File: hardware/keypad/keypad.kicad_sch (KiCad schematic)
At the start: 7 parts, among them J101 Conn_02x05_Odd_Even

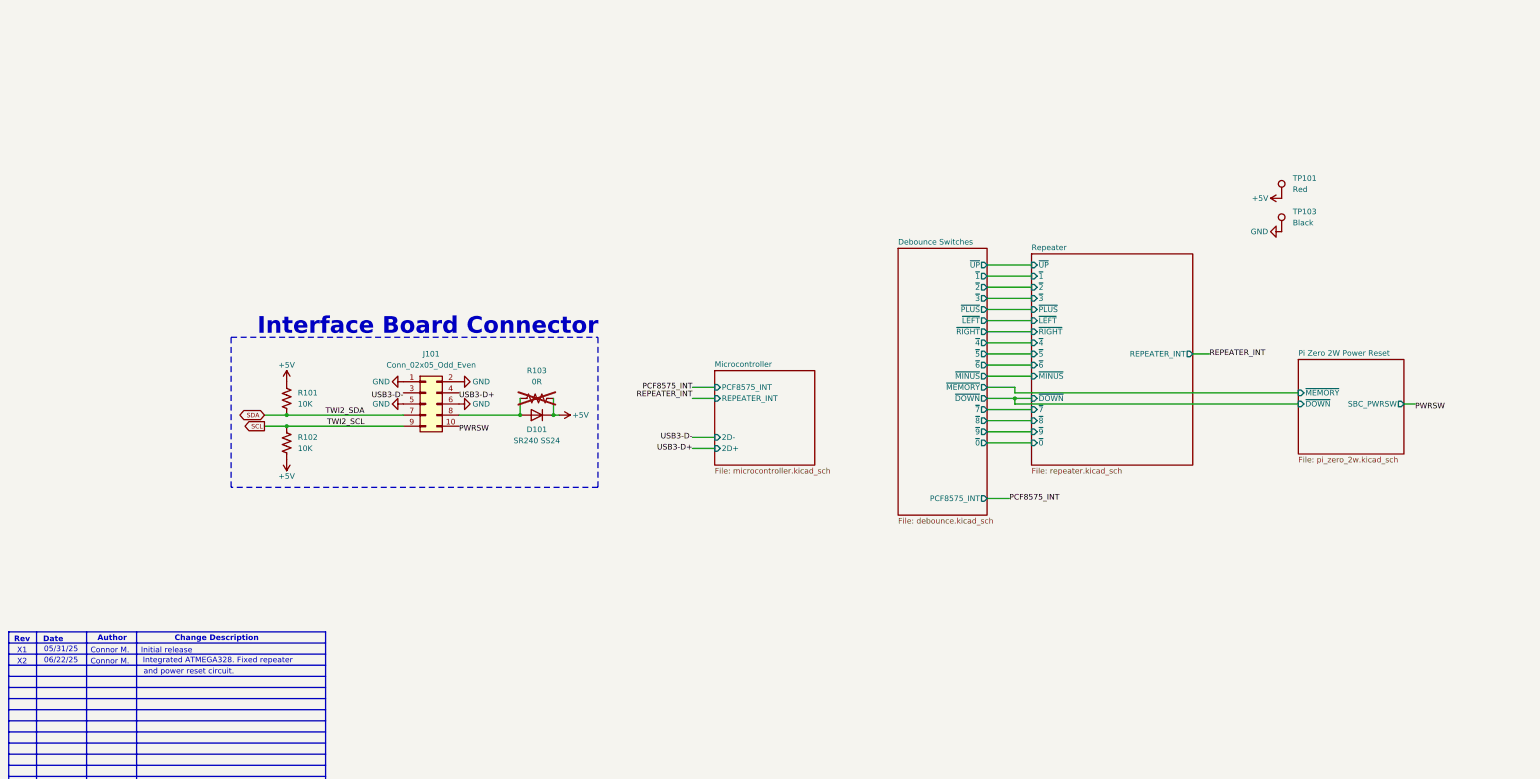
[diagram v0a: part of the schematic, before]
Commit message: [fix] repeater and sbc shutdown circuit
Fixed repeater and SBC shutdown circuit. Switched +5V VCC to +3.3V. Added C211
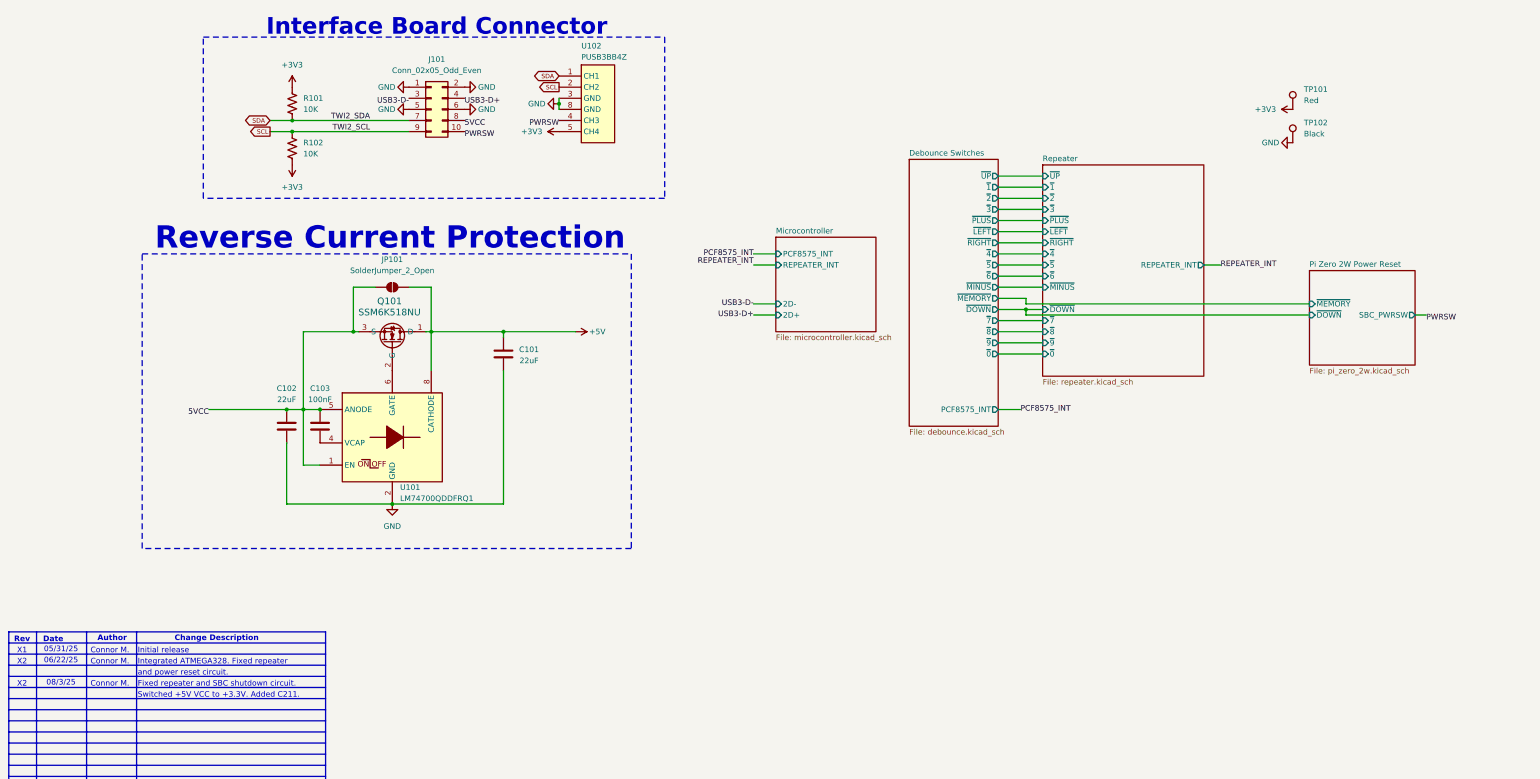
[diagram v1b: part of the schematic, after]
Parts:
- removed D101: SR240 SS24, Diode_SMD:D_SMA, symbol Device:D
- removed R103: 0R, Resistor_SMD:R_0805_2012Metric, symbol Device:R_US
- added C101, C102: 22uF, Capacitor_SMD:C_1206_3216Metric, symbol Device:C
- added C103: 100nF, Capacitor_SMD:C_1206_3216Metric, symbol Device:C
- added JP101: SolderJumper_2_Open, Jumper:SolderJumper-2_P1.3mm_Open_TrianglePad1.0x1.5mm, symbol Jumper:SolderJumper_2_Open
- added Q101: SSM6K518NU, SSM6K518NU:SOT-1220UDFN6B_TOS, symbol SSM6K518NU:SSM6K518NU
- added U101: LM74700QDDFRQ1, LM74700QDDFRQ1:SOT65P280X110-8N, symbol LM74700QDDFRQ1:LM74700QDDFRQ1
- added U102: PUSB3BB4Z, PUSB3BB4Z:SON50P100X250X50-10N, symbol PUSB3BB4Z:PUSB3BB4Z
- renumbered TP103 to TP102
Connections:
- net +5V: now also C101.1, JP101.2 (B), Q101.1 (D), U101.8 (CATHODE); no longer R101.1, R102.2, TP101.1
- net GND: now also C101.2, C102.2, U101.2 (GND), U102.3 (GND), U102.8 (GND)
- net PWRSW: now also U102.4 (CH3)
- net SCL: now also U102.2 (CH2)
- net SDA: now also U102.1 (CH1)
- net 5VCC: now reaches J101.8 (Pin_8)
- net 5VCC: now also C102.1, C103.1, JP101.1 (A), Q101.3 (S), U101.1 (EN), U101.5 (ANODE)
- new net: Q101.2 (G), U101.6 (GATE)
- new net: C103.2, U101.4 (VCAP)
- new net +3V3: R101.1, R102.2, TP101.1, U102.5 (CH4)
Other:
- note added: "08/3/25"
- note added: "Fixed repeater and SBC shutdown circuit."
- note added: "Reverse Current Protection"
- note added: "Switched +5V VCC to +3.3V. Added C211."
- moved on the sheet: J101, R101, R102, TP101, TP102
